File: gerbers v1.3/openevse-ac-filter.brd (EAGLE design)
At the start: 48.4 x 23 mm, 8 parts

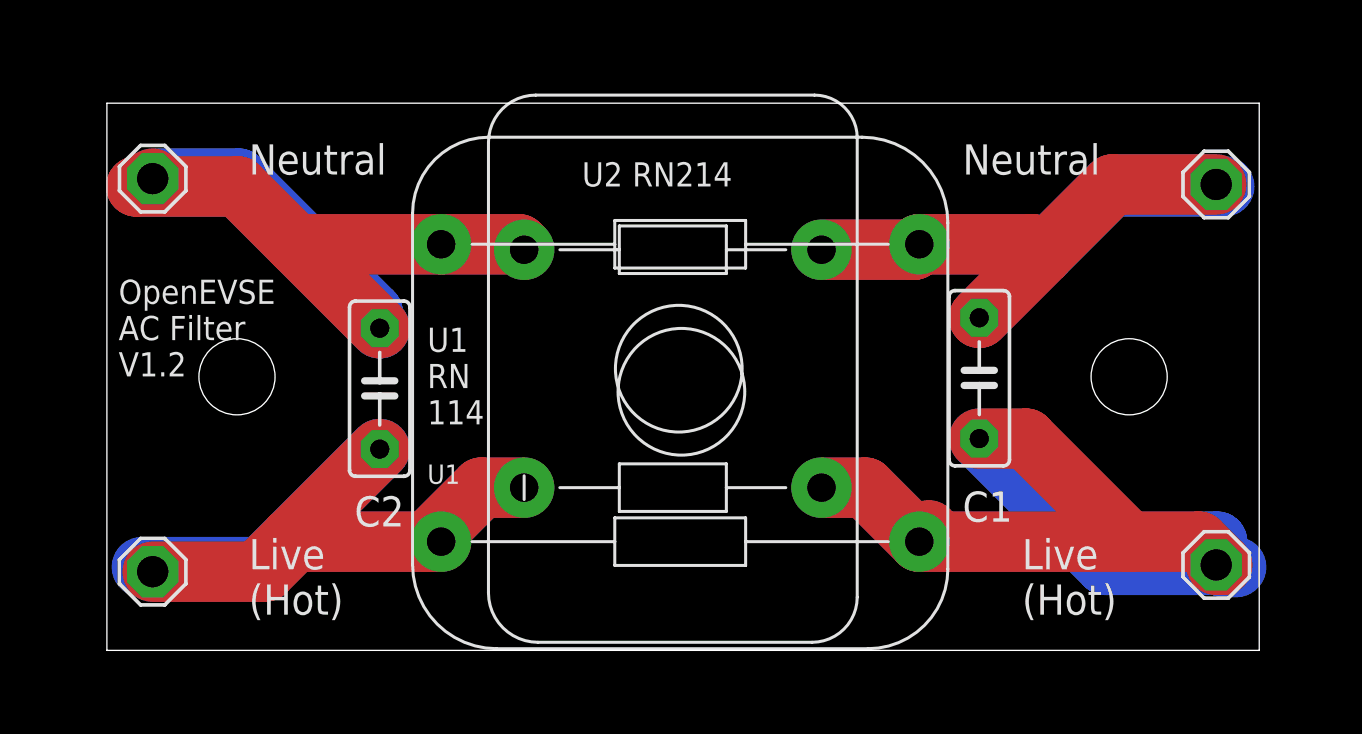
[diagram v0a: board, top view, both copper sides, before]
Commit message: V1.3 with terminal blocks
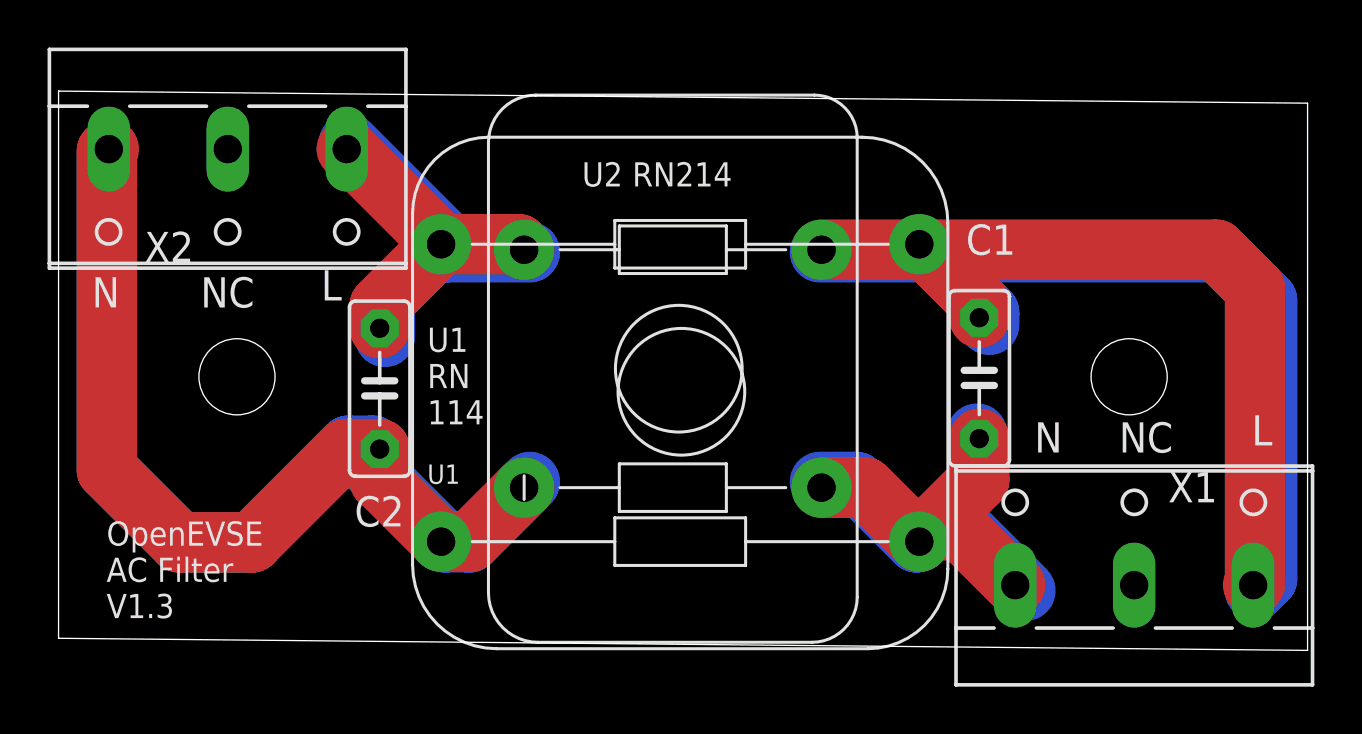
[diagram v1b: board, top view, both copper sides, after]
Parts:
- removed LSP2, LSP3, LSP4, LSP5: SE13, solpad:SE13
- added X1, X2: (no value), con-wago-500:W237-103
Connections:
- net N$1: now also X1.1; no longer LSP2.MP
- net N$2: now also X1.3; no longer LSP3.MP
- net N$3: now also X2.3; no longer LSP5.MP
- net N$4: now also X2.1; no longer LSP4.MP
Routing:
- net N$1: track 52.8 -> 15.0 mm
- net N$11: track 0.00 -> 36.1 mm
- net N$7: track 23.4 -> 0.00 mm
- net N$8: track 22.2 -> 0.00 mm
- net N$4: track 35.5 -> 13.8 mm
- net N$6: track 22.1 -> 37.3 mm
- net N$9: track 0.00 -> 10.9 mm
- net N$12: track 0.00 -> 10.7 mm
- net N$5: track 7.06 -> 0.00 mm
- net N$13: track 0.00 -> 4.31 mm
- net N$10: track 0.00 -> 4.27 mm
- net N$2: track 37.9 -> 35.4 mm
- net N$3: track 36.6 -> 37.3 mm
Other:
- board size 48.4 x 23 mm -> 52.5 x 23.5 mm
- board text added: "L"
- board text added: "N"
- board text added: "NC"
- board text added: "OpenEVSE AC Filter V1.3"
- board text removed: "Live (Hot)"
- board text removed: "Neutral"
- board text removed: "OpenEVSE AC Filter V1.2"
